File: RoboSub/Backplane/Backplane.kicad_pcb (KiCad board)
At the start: 2 copper layers, 122 x 86 mm, 45 parts, among them J1 BatteryIn, J10 motor4, J11 motor5, J12 motor6, J13 JetsonPWR, J14 JetsonCAN, J15 SWD_UART, J2 I2C, J3 Spine, J4 Spine, J5 Spine, J6 IMU, J7 motor1, J8 motor2, J9 motor3, M1 ESCB, M2 ESCB, M3 ESCB, M4 ESCB, M5 ESCB, M6 ESCB, SW1 DBG2, SW2 DBG1, SW3 RST, U1 TCAN330G, U2 STM32G0B1KxTxN, U3 TCAN330G

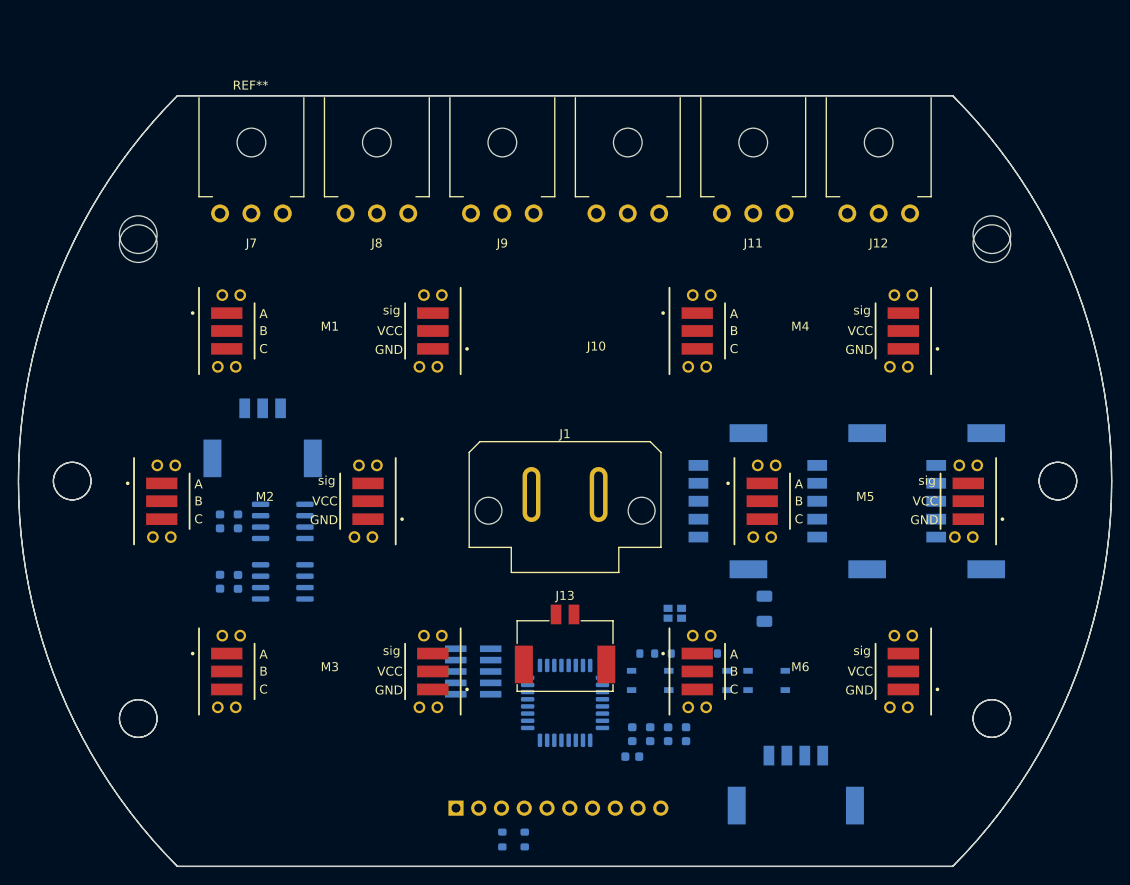
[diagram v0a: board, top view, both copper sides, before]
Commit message: first backplane layout commit
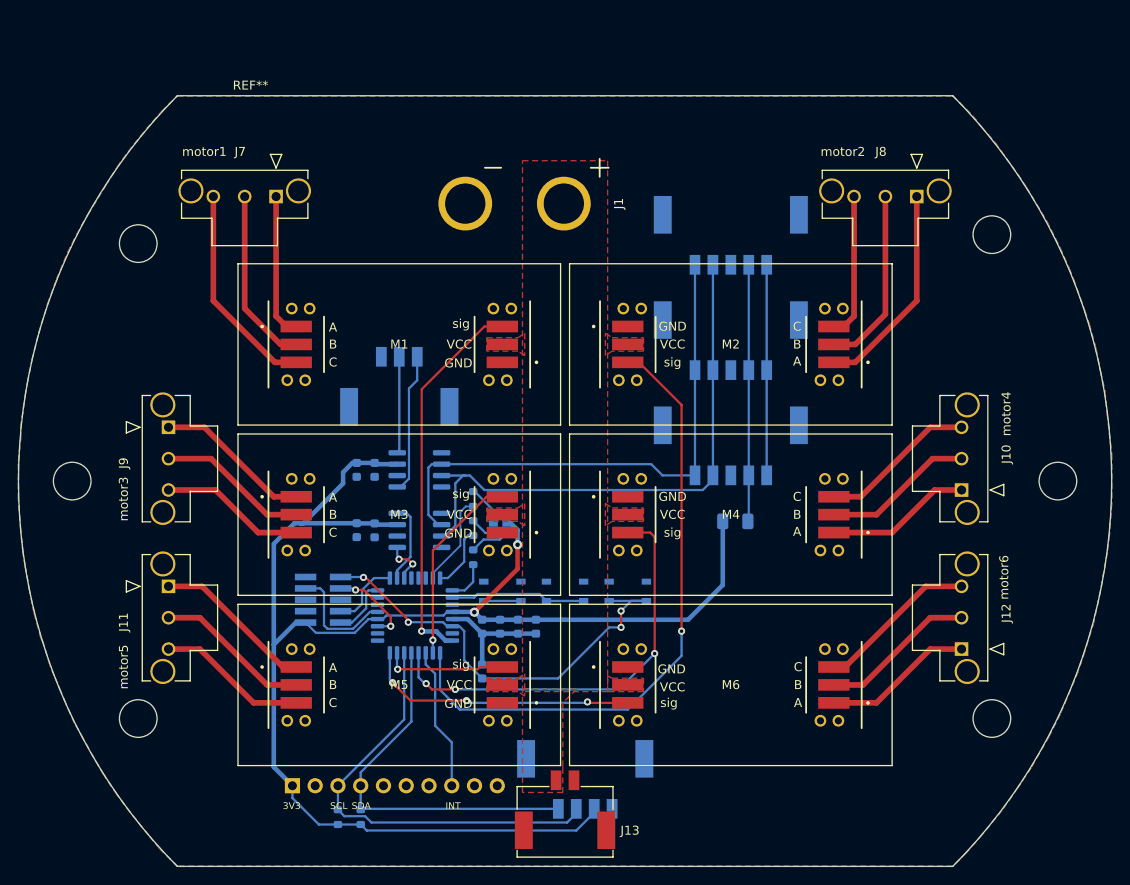
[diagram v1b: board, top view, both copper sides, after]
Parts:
- removed the REF** at (150.0, 100.0)
- added G***: LOGO, extraparts:auv_logo, B.Cu at (185.5, 136.2)
- J1: footprint extraparts:Molex_SuperSabre_Vert_2pin -> urbparts:Conn_XT90
- J10, J11, J12, J7, J8, J9: footprint extraparts:Molex_UltraFit_RH_3pin -> extraparts:Molex_UltraFit_Vert_3pin
- moved J11 85.2 mm to (105.7, 111.8), turned to -90 degrees
- moved J12 62.5 mm to (194.2, 118.8), turned to 90 degrees
- moved J8 61.3 mm to (189.2, 68.2)
- moved J10 57.7 mm to (194.2, 101.0), turned to 90 degrees
- moved M5 55.9 mm to (131.5, 122.8)
- moved M2 54.9 mm to (168.5, 84.8), turned to 180 degrees
- moved J9 52.5 mm to (105.7, 94.0), turned to -90 degrees
- moved J5 47.1 mm to (168.5, 67.3), turned to 0 degrees
- moved J1 32.5 mm to (149.9, 69.0), turned to 90 degrees
- moved J4 29.5 mm to (168.5, 79.0), turned to 0 degrees
- moved R1 28.5 mm to (139.8, 108.5), turned to 90 degrees
- moved R2 26.9 mm to (139.8, 105.2), turned to 90 degrees
- moved J2 26.0 mm to (152.2, 128.0), turned to 0 degrees
- moved R3 26.0 mm to (139.8, 102.0), turned to 90 degrees
- moved M4 21.9 mm to (168.5, 103.8), turned to 180 degrees
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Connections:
- J10 pad : (no net) -> GND
- J11 pad : (no net) -> GND
- J12 pad : (no net) -> GND
- J13 pad MP: (no net) -> GND
- J14 pad MP: (no net) -> GND
- J2 pad MP: (no net) -> GND
- J3 pad MP: (no net) -> GND
- J4 pad MP: (no net) -> GND
- J5 pad MP: (no net) -> GND
- J7 pad : (no net) -> GND
- J8 pad : (no net) -> GND
- J9 pad : (no net) -> GND
- M1 pad : (no net) -> GND
- M2 pad : (no net) -> GND
- M3 pad : (no net) -> GND
- M4 pad : (no net) -> GND
- M5 pad : (no net) -> GND
- M6 pad : (no net) -> GND
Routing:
- net +3V3: track 0.00 -> 169.3 mm, vias 0 -> 2
- net /MOTOR2: track 0.00 -> 70.4 mm, vias 0 -> 1
- net /CANH: track 0.00 -> 63.6 mm
- net /CANL: track 0.00 -> 61.1 mm
- net /RST: track 0.00 -> 49.7 mm, vias 0 -> 4
- net /SCL: track 0.00 -> 48.7 mm
- net /MOTOR4: track 0.00 -> 47.5 mm, vias 0 -> 3
- net /MOTOR1: track 0.00 -> 42.8 mm, vias 0 -> 1
- net /SDA: track 0.00 -> 41.9 mm
- net /MOTOR6: track 0.00 -> 30.7 mm, vias 0 -> 3
- net Net-(F1-Pad2): track 0.00 -> 28.7 mm
- net Net-(J7-Pad3): track 0.00 -> 23.7 mm
- net Net-(J8-Pad1): track 0.00 -> 23.7 mm
- net Net-(J3-Pad1): track 0.00 -> 23.5 mm
- net /MOTOR3: track 0.00 -> 21.7 mm, vias 0 -> 1
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- added copper zone on F.Cu, net +BATT
- added copper zone on B.Cu, net GND
- added copper zone on F.Cu, net GND
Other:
- board text added: "3V3"
- board text added: "INT"
- board text added: "SCL"
- board text added: "SDA"
- board text added: "Suphakorn L"

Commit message: made changes to blackplane layout second commit
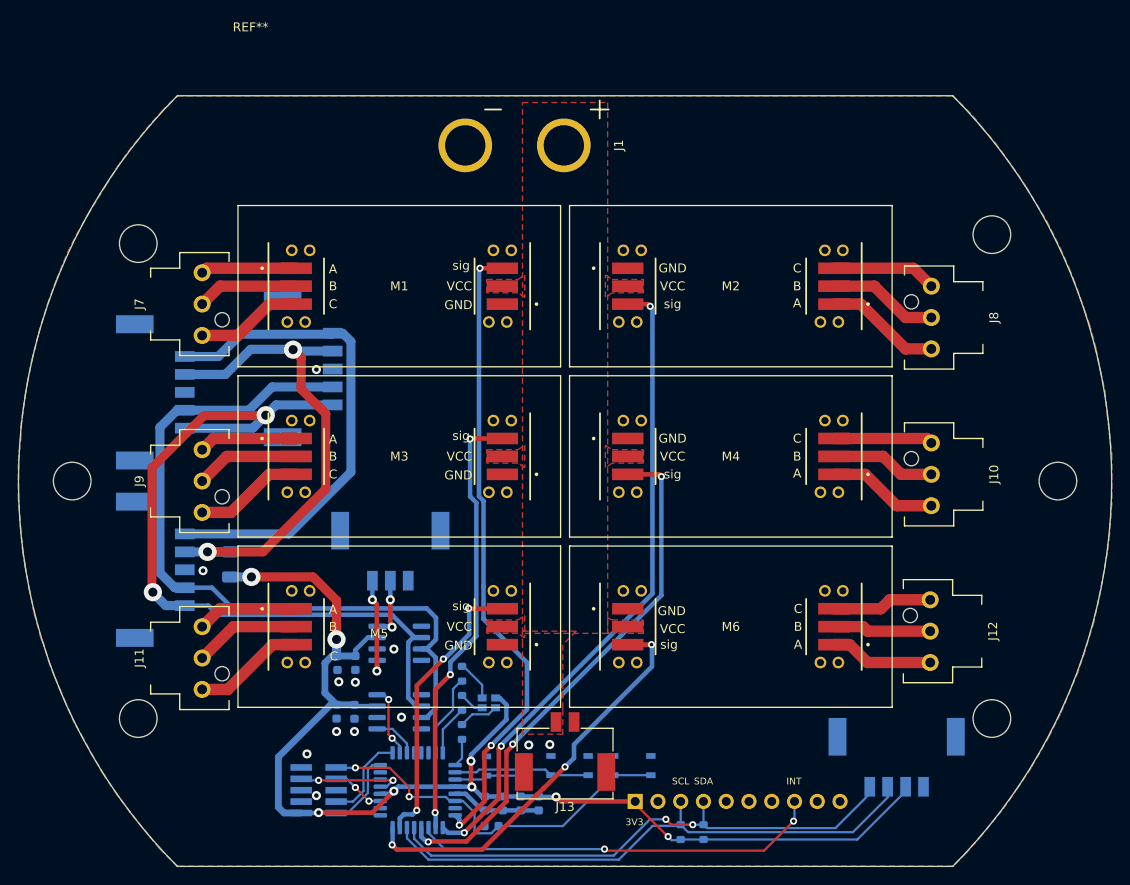
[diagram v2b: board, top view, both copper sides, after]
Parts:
- removed G***: LOGO, extraparts:auv_logo
- J10, J11, J12, J7, J8, J9: footprint extraparts:Molex_UltraFit_Vert_3pin -> extraparts:Molex_UltraFit_KP_Vert_3pin
- moved J3 72.1 mm to (99.0, 109.9), turned to 90 degrees
- moved J4 70.4 mm to (99.0, 90.1), turned to 90 degrees
- moved J5 56.7 mm to (115.5, 87.5), turned to 90 degrees
- moved F1 56.6 mm to (112.6, 109.3), turned to 90 degrees
- moved J6 38.3 mm to (157.8, 135.8)
- moved R4 38.3 mm to (162.9, 139.2)
- moved R5 38.3 mm to (165.4, 139.2)
- moved J2 34.8 mm to (187.0, 125.5)
- moved C8 21.7 mm to (126.6, 120.3)
- moved C9 21.7 mm to (124.6, 120.3)
- moved J15 21.3 mm to (122.5, 134.5)
- moved C1 20.4 mm to (126.5, 125.8)
- moved C2 20.4 mm to (124.5, 125.7)
- moved U1 20.4 mm to (131.5, 125.8)
- moved C4 19.7 mm to (141.1, 136.0)
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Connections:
- J10 pad : GND -> (no net)
- J11 pad : GND -> (no net)
- J12 pad : GND -> (no net)
- J7 pad : GND -> (no net)
- J8 pad : GND -> (no net)
- J9 pad : GND -> (no net)
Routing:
- net Net-(J3-Pad1): track 23.5 -> 56.0 mm
- net /INT: track 16.0 -> 45.8 mm, vias 0 -> 2
- net /MOTOR1: track 42.8 -> 71.4 mm, vias 1 -> 3
- net +3V3: track 169.3 -> 141.8 mm, vias 2 -> 8
- net /MOTOR3: track 21.7 -> 49.2 mm, vias 1 -> 3
- net /CANL: track 61.1 -> 88.5 mm, vias 0 -> 2
- net Net-(F1-Pad2): track 28.7 -> 55.9 mm, vias 0 -> 2
- net /CANH: track 63.6 -> 85.1 mm
- net /SDA: track 41.9 -> 59.9 mm, vias 0 -> 2
- net /MOTOR5: track 14.8 -> 32.1 mm, vias 1 -> 3
- net /MOTOR6: track 30.7 -> 45.6 mm
- net /SCL: track 48.7 -> 63.1 mm
- net /MOTOR4: track 47.5 -> 59.9 mm
- net Net-(J7-Pad3): track 23.7 -> 11.9 mm
- net Net-(J8-Pad1): track 23.7 -> 12.9 mm
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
